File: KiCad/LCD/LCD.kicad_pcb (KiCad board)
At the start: 2 copper layers, 15 x 67 mm, 12 parts, among them J1 Conn_01x10, J2 LCD, U1 L7812

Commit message: finish schematic and start board layout
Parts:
- moved J2 4.22 mm to (171.4, 74.2)
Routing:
- net /~CS: track 4.62 -> 13.9 mm
- net /D/~C: track 9.79 -> 4.95 mm
- net /~RST: track 10.00 -> 5.89 mm, vias 1 -> 0
- net +3V3: track 24.3 -> 20.4 mm
- net Net-(J2-Pad24): track 25.7 -> 29.6 mm
- net Net-(C3-Pad1): track 60.3 -> 63.7 mm
- net +12V: track 80.8 -> 84.1 mm
- net /MOSI: track 4.54 -> 7.80 mm
- net /SCK: track 4.61 -> 6.30 mm

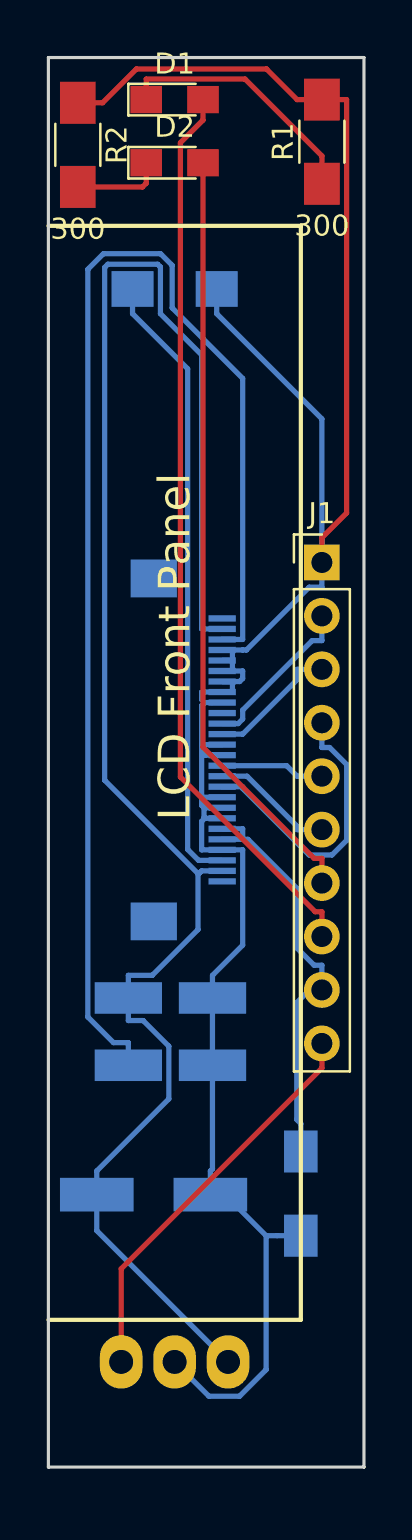
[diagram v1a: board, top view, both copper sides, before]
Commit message: start board routing
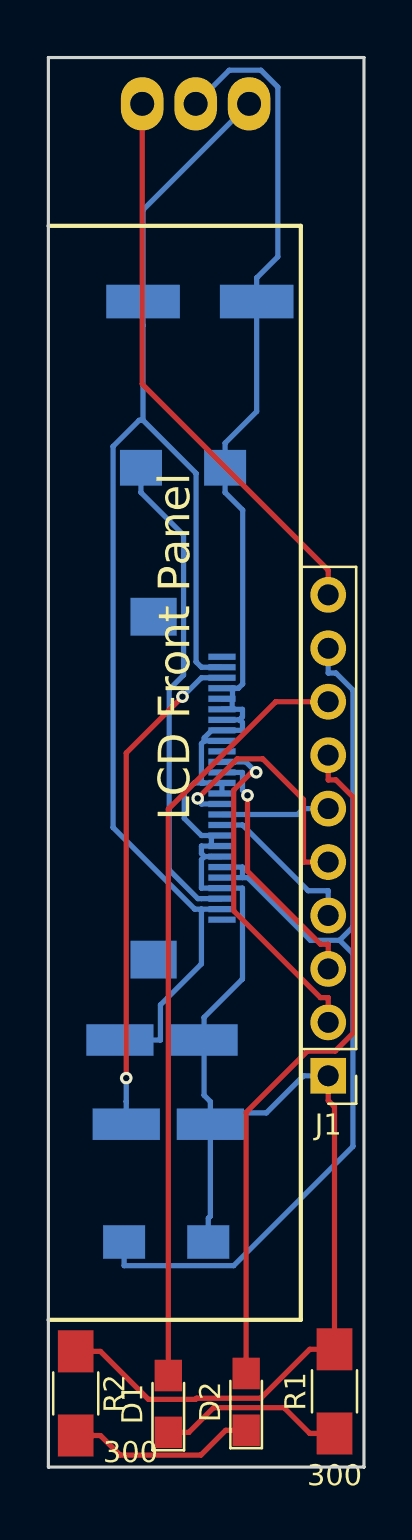
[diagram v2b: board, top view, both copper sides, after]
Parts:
- moved D1 62.0 mm to (170.7, 104.0), turned to 90 degrees
- moved U1 59.8 mm to (172.0, 42.2)
- moved R1 59.4 mm to (178.6, 103.4)
- moved R2 59.4 mm to (166.3, 103.5)
- moved D2 59.0 mm to (174.4, 103.9), turned to 90 degrees
- moved C1 42.5 mm to (172.2, 51.6)
- moved J1 24.4 mm to (178.3, 88.4), turned to 180 degrees
- moved R3 8.51 mm to (171.4, 59.5)
- moved C4 6.80 mm to (170.6, 96.3), turned to 0 degrees
- moved C3 2.80 mm to (170.7, 90.7)
- moved C2 2.04 mm to (170.4, 86.7)
- moved J2 1.82 mm to (171.4, 76.0)
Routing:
- net Net-(C3-Pad1): track 63.7 -> 23.7 mm, vias 0 -> 2
- net +3V3: track 20.4 -> 47.6 mm
- net +12V: track 84.1 -> 66.8 mm
- net /MOSI: track 7.80 -> 16.4 mm, vias 0 -> 1
- net +24V: track 19.1 -> 27.0 mm
- net /D/~C: track 4.95 -> 12.1 mm, vias 0 -> 1
- net Net-(D1-Pad2): track 43.2 -> 36.6 mm
- net /~CS: track 13.9 -> 7.52 mm
- net Net-(J2-Pad24): track 29.6 -> 23.3 mm
- net /SCK: track 6.30 -> 12.2 mm, vias 0 -> 1
- net GND: track 114.0 -> 108.8 mm
- net Net-(D2-Pad1): track 4.30 -> 8.97 mm
- net Net-(D2-Pad2): track 36.8 -> 33.0 mm
- net Net-(D1-Pad1): track 12.2 -> 8.89 mm
- net /~RST: track 5.89 -> 5.17 mm

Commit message: save all files for LCD
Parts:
- removed C2, C3: 4.7u, Capacitors_Tantalum_SMD:CP_Tantalum_Case-A_EIA-3216-18_Hand
- removed C4: .1u, Capacitors_SMD:C_1206_HandSoldering
- removed R3: 680k, Resistors_SMD:R_1206_HandSoldering
- removed U1: L7812, Power_Integrations:TO-220
- C1: value 100uF -> 1uf; footprint Capacitors_SMD:CP_Elec_6.3x5.3 -> Capacitor_SMD:C_1206_3216Metric
- J1: moved to B.Cu
- J2: value LCD -> Conn_01x12; footprint Connector_FFC-FPC:REVHirose_FH12-26S-0.5SH_1x26-1MP_P0.50mm_Horizontal -> Connector_FFC-FPC:Hirose_FH12-11S-0.5SH_1x11-1MP_P0.50mm_Horizontal
- R1, R2: value 300 -> R
- moved J2 22.8 mm to (171.4, 53.2), turned to 0 degrees
- moved C1 21.6 mm to (170.4, 73.1)
- turned J1 to 0 degrees
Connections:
- C1 pad 1: +12V -> +3V3
- J1 pad 10: +24V -> Net-(J1-Pad10)
- J1 pad 2: /MOSI -> Net-(J1-Pad2)
- J1 pad 3: /SCK -> Net-(J1-Pad3)
- J1 pad 4: /~CS -> Net-(J1-Pad4)
- J1 pad 5: /D/~C -> Net-(J1-Pad5)
- J1 pad 6: /~RST -> Net-(J1-Pad6)
- J2 pad 1: Net-(J2-Pad1) -> GND
- J2 pad 10: Net-(J2-Pad10) -> +3V3
- J2 pad 11: /MOSI -> +3V3
- J2 pad 2: +12V -> Net-(J2-Pad2)
- J2 pad 3: Net-(C3-Pad1) -> Net-(J1-Pad2)
- J2 pad 4: GND -> Net-(J1-Pad3)
- J2 pad 5: GND -> Net-(J1-Pad5)
- J2 pad 6: GND -> Net-(J1-Pad6)
- J2 pad 7: GND -> Net-(J1-Pad4)
- R1 pad 1: Net-(D1-Pad1) -> GND
- R1 pad 2: GND -> Net-(D1-Pad1)
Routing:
- net +12V: track 66.8 -> 0.00 mm
- net Net-(J1-Pad2): track 0.00 -> 37.2 mm
- net Net-(J1-Pad5): track 0.00 -> 35.5 mm
- net Net-(J1-Pad3): track 0.00 -> 34.9 mm
- net Net-(J1-Pad6): track 0.00 -> 32.6 mm
- net Net-(D1-Pad1): track 8.89 -> 39.2 mm
- net Net-(J1-Pad4): track 0.00 -> 30.2 mm, vias 0 -> 1
- net +24V: track 27.0 -> 0.00 mm
- net Net-(C3-Pad1): track 23.7 -> 0.00 mm, vias 2 -> 0
- net Net-(J2-Pad24): track 23.3 -> 0.00 mm
- net +3V3: track 47.6 -> 25.9 mm
- net GND: track 108.8 -> 129.5 mm, vias 0 -> 2
- net /MOSI: track 16.4 -> 0.00 mm, vias 1 -> 0
- net /SCK: track 12.2 -> 0.00 mm, vias 1 -> 0
- net /D/~C: track 12.1 -> 0.00 mm, vias 1 -> 0
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
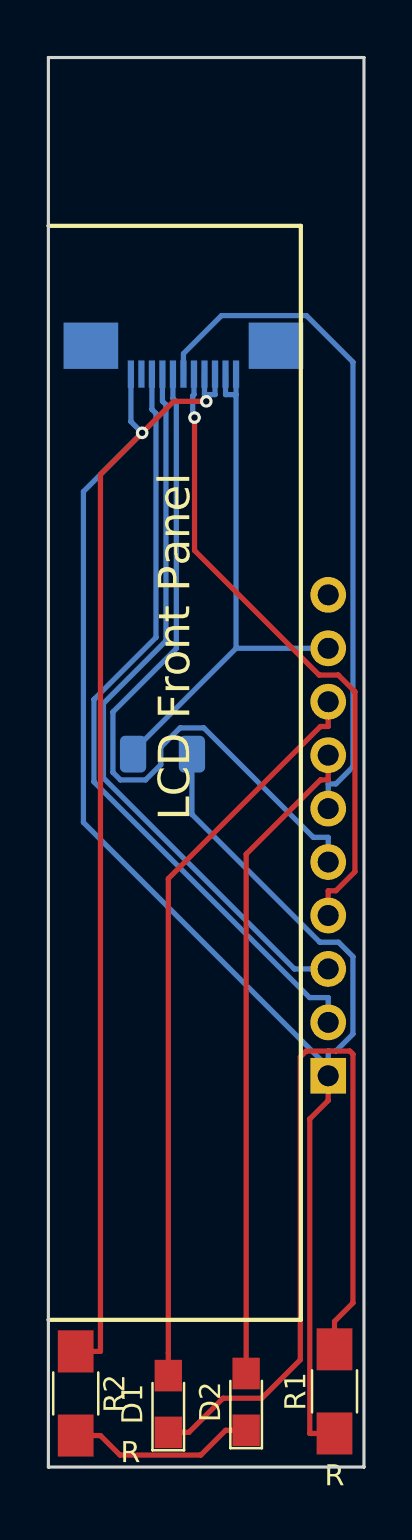
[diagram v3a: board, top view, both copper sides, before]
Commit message: added everything for latest version of the LCD screen
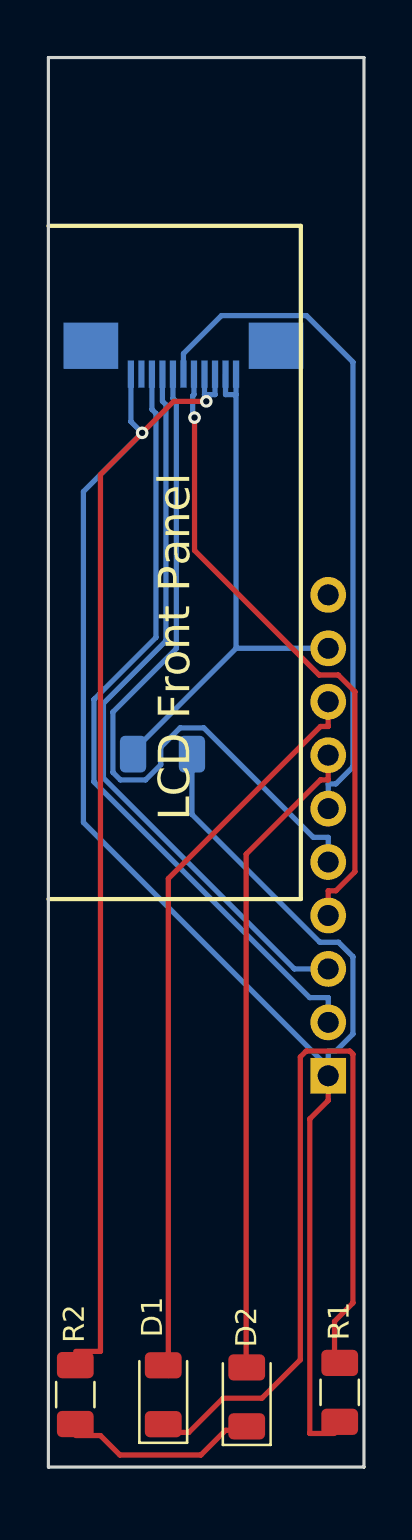
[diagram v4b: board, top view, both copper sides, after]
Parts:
- D1, D2: footprint LEDs:LED_0805_HandSoldering -> LED_SMD:LED_1206_3216Metric
- R1, R2: value R -> 300; footprint Resistors_SMD:R_1206_HandSoldering -> Resistor_SMD:R_1206_3216Metric
- moved D1 0.50 mm to (170.5, 103.6)
- moved R1 0.25 mm to (178.8, 103.4)
- moved D2 0.24 mm to (174.4, 103.7)
- moved R2 0.06 mm to (166.3, 103.6)

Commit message: move changes back in to device
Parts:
- J2: footprint Connector_FFC-FPC:Hirose_FH12-11S-0.5SH_1x11-1MP_P0.50mm_Horizontal -> Connector_FFC-FPC:Hirose_FH12-12S-0.5SH_1x12-1MP_P0.50mm_Horizontal
- moved J2 0.55 mm to (171.7, 52.7)
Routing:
- net GND: track 129.5 -> 132.9 mm
